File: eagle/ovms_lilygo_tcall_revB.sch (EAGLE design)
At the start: 45 parts, among them IC2 SN65HVD233, IC3 SN65HVD233, IC4 LMR516XX, IC5 MCP2515, Q1 X49SM16MSD2SC

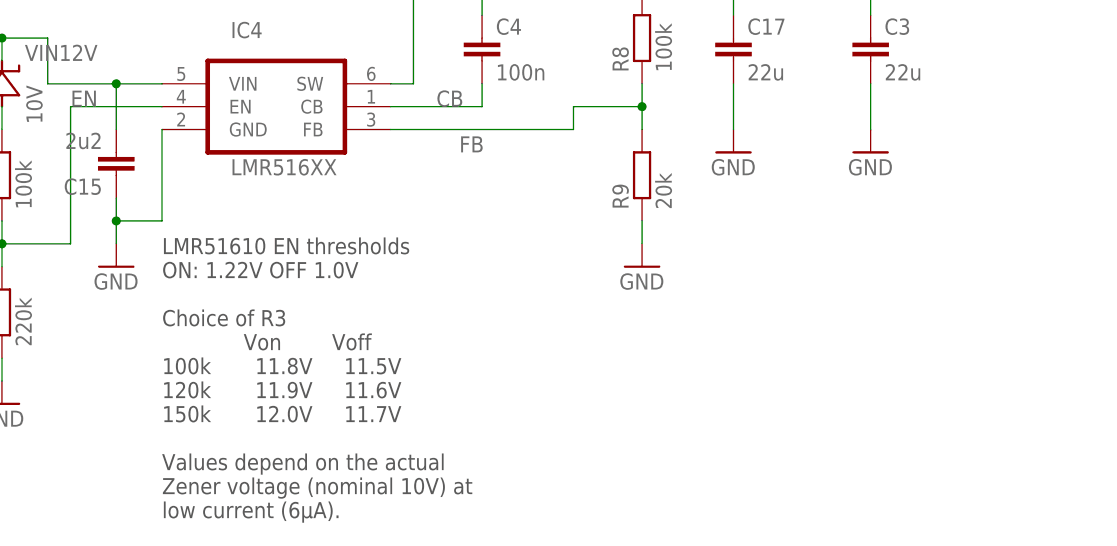
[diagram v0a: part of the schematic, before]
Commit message: Change schematic to increase default DCDC output voltage
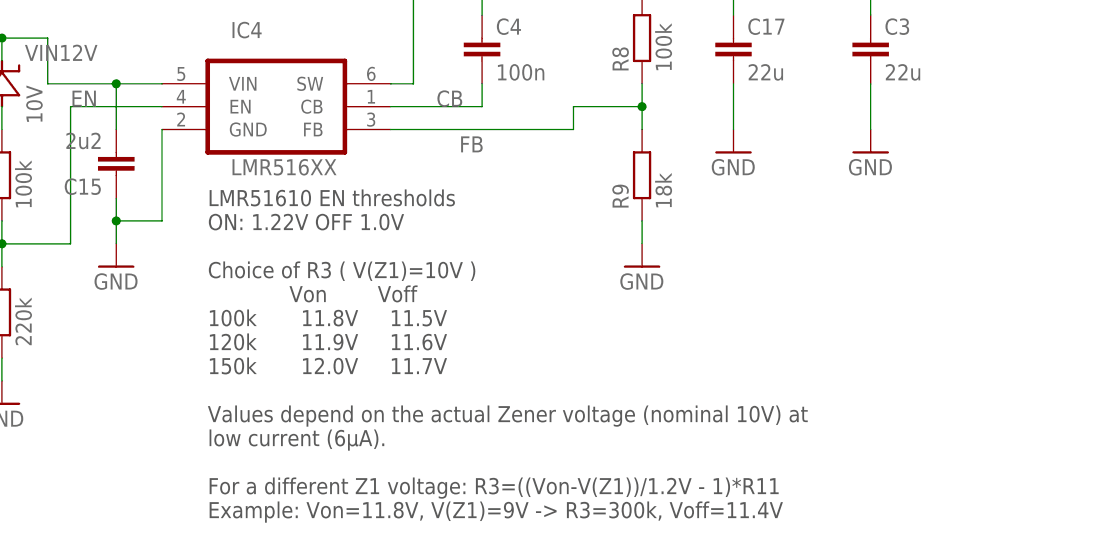
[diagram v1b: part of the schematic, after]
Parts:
- R9: value 20k -> 18k
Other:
- note added: "LMR51610 EN thresholds ON: 1.22V OFF 1.0V Choice of R3 ( V(Z1)=10V ) Von Voff 100k 11.8V 11.5V 120k 11.9V 11.6V 150k 12.0V 11.7V Values depend on the actual Zener voltage (nominal 10V) at low current (6µA). For a different Z1 voltage: R3=((Von-V(Z1))/1.2V - 1)*R11 Example: Von=11.8V, V(Z1)=9V -> R3=300k, Voff=11.4V"
- note removed: "LMR51610 EN thresholds ON: 1.22V OFF 1.0V Choice of R3 Von Voff 100k 11.8V 11.5V 120k 11.9V 11.6V 150k 12.0V 11.7V Values depend on the actual Zener voltage (nominal 10V) at low current (6µA)."
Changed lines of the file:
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@@
 <part name="GND10" library="supply1" deviceset="GND" device=""/>
 <part name="R8" library="rcl" library_urn="urn:adsk.eagle:library:334" deviceset="R-EU_" device="M0805" package3d_urn="urn:adsk.eagle:package:23556/2" value="100k"/>
-<part name="R9" library="rcl" library_urn="urn:adsk.eagle:library:334" deviceset="R-EU_" device="M0805" package3d_urn="urn:adsk.eagle:package:23556/2" value="20k"/>
+<part name="R9" library="rcl" library_urn="urn:adsk.eagle:library:334" deviceset="R-EU_" device="M0805" package3d_urn="urn:adsk.eagle:package:23556/2" value="18k"/>
 <part name="GND12" library="supply1" deviceset="GND" device=""/>
 <part name="R11" library="rcl" library_urn="urn:adsk.eagle:library:334" deviceset="R-EU_" device="M0805" package3d_urn="urn:adsk.eagle:package:23556/2" value="220k"/>
@@
 P9 - +12V
  </text>
-<text x="-119.38" y="-38.1" size="1.778" layer="97">LMR51610 EN thresholds
+<text x="-114.3" y="-38.1" size="1.778" layer="97">LMR51610 EN thresholds
 ON: 1.22V OFF 1.0V
-Choice of R3
+Choice of R3 ( V(Z1)=10V )
              Von        Voff
 100k       11.8V     11.5V
 120k       11.9V     11.6V
 150k       12.0V     11.7V
-Values depend on the actual
-Zener voltage (nominal 10V) at
-low current (6µA). </text>
+Values depend on the actual Zener voltage (nominal 10V) at
+low current (6µA).
+For a different Z1 voltage: R3=((Von-V(Z1))/1.2V - 1)*R11
+Example: Von=11.8V, V(Z1)=9V -&gt; R3=300k, Voff=11.4V </text>
 </plain>
 <instances>

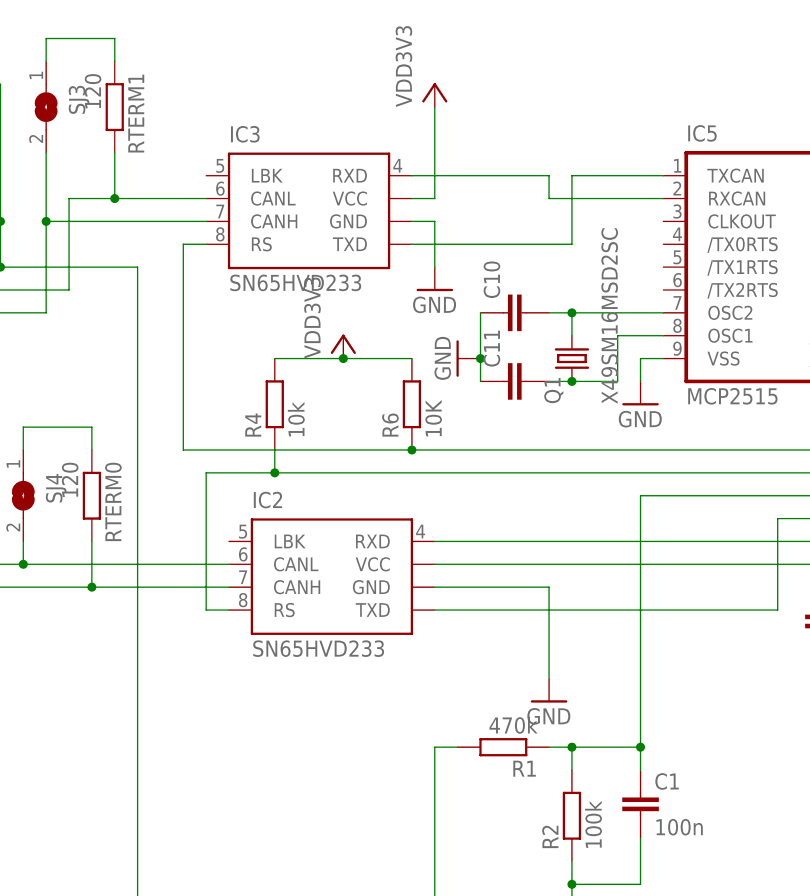
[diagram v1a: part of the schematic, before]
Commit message: Replace CAN transceiver (TCAN330)
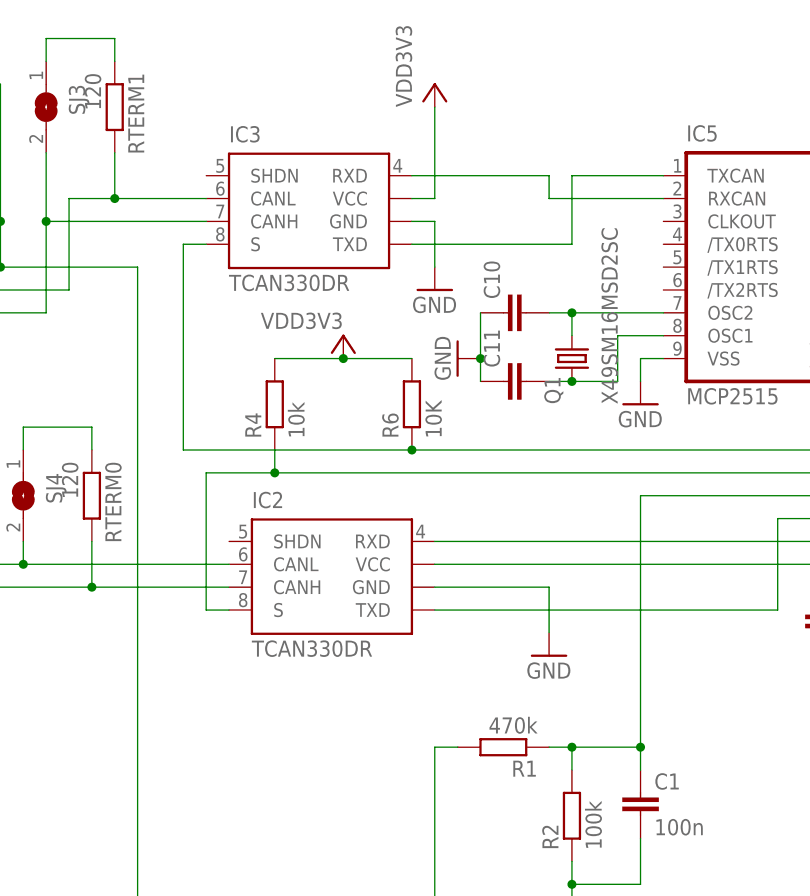
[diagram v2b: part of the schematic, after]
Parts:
- IC2, IC3: value SN65HVD233 -> TCAN330DR; device ovms_lilygo:SN65HVD23XS -> ovms_lilygo:TCAN330DRS
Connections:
- net N$15: now also IC2.S; no longer IC2.RS
- net N$6: now also IC3.S; no longer IC3.RS
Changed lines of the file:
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@@
 <part name="C3" library="rcl" library_urn="urn:adsk.eagle:library:334" deviceset="C-EU" device="C0805K" package3d_urn="urn:adsk.eagle:package:23681/2" value="22u"/>
 <part name="C6" library="rcl" library_urn="urn:adsk.eagle:library:334" deviceset="C-EU" device="C0805K" package3d_urn="urn:adsk.eagle:package:23681/2" value="100n"/>
-<part name="IC2" library="ovms_lilygo" deviceset="SN65HVD23X" device="S" value="SN65HVD233"/>
-<part name="IC3" library="ovms_lilygo" deviceset="SN65HVD23X" device="S" value="SN65HVD233"/>
+<part name="IC2" library="ovms_lilygo" deviceset="TCAN330DR" device="S" value="TCAN330DR"/>
+<part name="IC3" library="ovms_lilygo" deviceset="TCAN330DR" device="S" value="TCAN330DR"/>
 <part name="R4" library="rcl" library_urn="urn:adsk.eagle:library:334" deviceset="R-EU_" device="M0805" package3d_urn="urn:adsk.eagle:package:23556/2" value="10k"/>
 <part name="P+2" library="supply1" library_urn="urn:adsk.eagle:library:371" deviceset="VCC" device="" value="VDD3V3"/>
@@
 <attribute name="VALUE" x="-149.86" y="-2.54" size="1.778" layer="96"/>
 </instance>
-<instance part="GND1" gate="1" x="-157.48" y="40.64" smashed="yes">
-<attribute name="VALUE" x="-160.02" y="38.1" size="1.778" layer="96"/>
+<instance part="GND1" gate="1" x="-157.48" y="45.72" smashed="yes">
+<attribute name="VALUE" x="-160.02" y="43.18" size="1.778" layer="96"/>
 </instance>
 <instance part="EXT_12V" gate="-1" x="-248.92" y="10.16" smashed="yes">
@@
 </instance>
 <instance part="P+2" gate="VCC" x="-180.34" y="81.28" smashed="yes">
-<attribute name="VALUE" x="-182.88" y="78.74" size="1.778" layer="96" rot="R90"/>
+<attribute name="VALUE" x="-180.34" y="83.82" size="1.778" layer="96" rot="R180"/>
 </instance>
 <instance part="GND8" gate="1" x="-147.32" y="73.66" smashed="yes">
@@
 <wire x1="-170.18" y1="53.34" x2="-157.48" y2="53.34" width="0.1524" layer="91"/>
 <pinref part="GND1" gate="1" pin="GND"/>
-<wire x1="-157.48" y1="43.18" x2="-157.48" y2="53.34" width="0.1524" layer="91"/>
+<wire x1="-157.48" y1="48.26" x2="-157.48" y2="53.34" width="0.1524" layer="91"/>
 <pinref part="IC2" gate="G$1" pin="GND"/>
 </segment>
@@
 <net name="N$6" class="0">
 <segment>
-<pinref part="IC3" gate="G$1" pin="RS"/>
+<pinref part="IC3" gate="G$1" pin="S"/>
 <wire x1="-195.58" y1="91.44" x2="-198.12" y2="91.44" width="0.1524" layer="91"/>
 <wire x1="-198.12" y1="91.44" x2="-198.12" y2="68.58" width="0.1524" layer="91"/>
@@
 <net name="N$15" class="0">
 <segment>
-<pinref part="IC2" gate="G$1" pin="RS"/>
+<pinref part="IC2" gate="G$1" pin="S"/>
 <wire x1="-193.04" y1="50.8" x2="-195.58" y2="50.8" width="0.1524" layer="91"/>
 <wire x1="-195.58" y1="50.8" x2="-195.58" y2="66.04" width="0.1524" layer="91"/>
